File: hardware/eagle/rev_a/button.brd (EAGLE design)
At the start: 74 x 40 mm, 13 parts

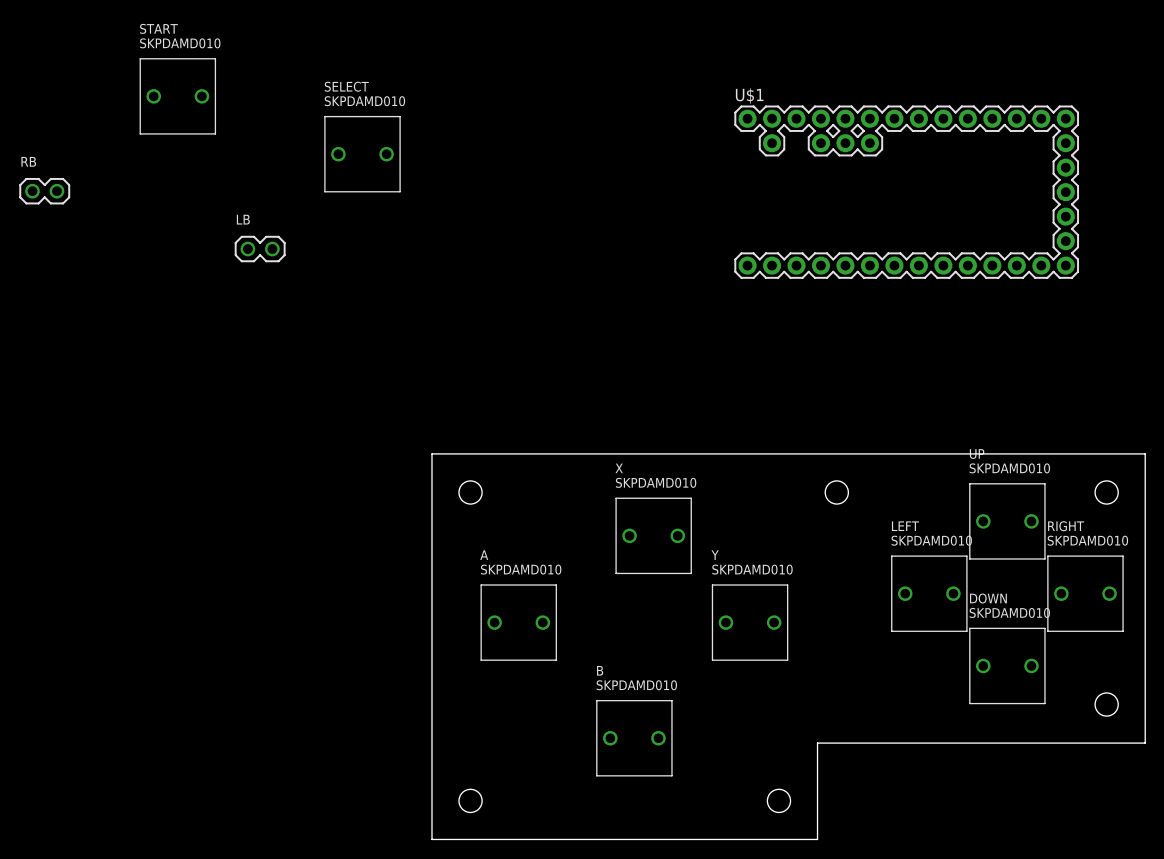
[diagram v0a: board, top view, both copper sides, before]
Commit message: First stab at button board Fits current body model, faceplate needs spacing of start/select
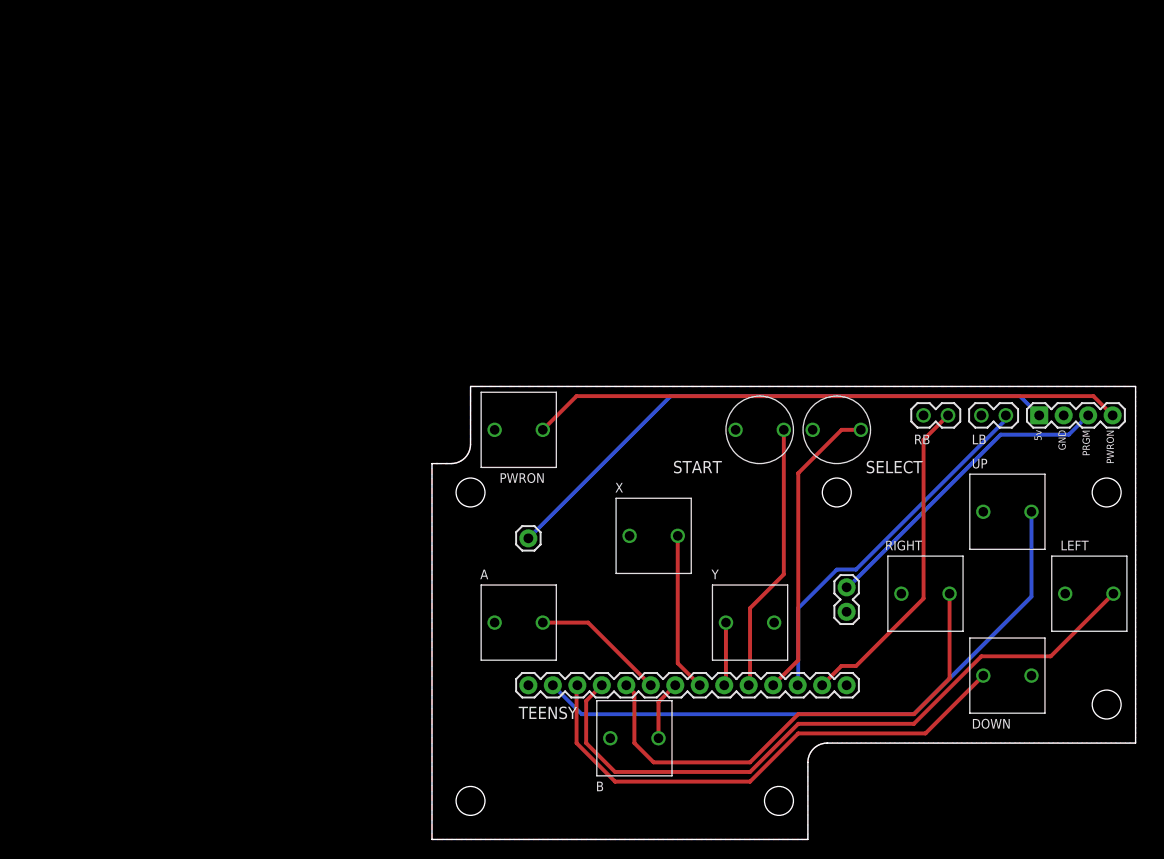
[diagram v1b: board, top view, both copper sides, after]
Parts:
- removed U$1: TEENSY_LC, BMO:TEENSY_LC
- added JP2: (no value), SparkFun-Connectors:1X04
- added PWRON: SKPDAMD010, switches:SKPDAMD010
- added TEENSY: TEENSY_LC, BMO:TEENSY_LC
- SELECT, START: value SKPDAMD010 -> EVQ11D09K; device switches:SKPDAMD010 -> BMO:EVQ11D09K
- moved RB 95.3 mm to (47.0, 40.0)
- moved LB 78.0 mm to (53.0, 40.0)
- moved START 69.6 mm to (30.0, 38.5)
- moved SELECT 56.9 mm to (38.0, 38.5)
- moved LEFT 16.6 mm to (64.2, 21.5)
- moved RIGHT 16.6 mm to (47.2, 21.5)
- moved DOWN 1.00 mm to (55.7, 13.0), turned to 180 degrees
- moved UP 1.00 mm to (55.7, 30.0)
- turned Y to 180 degrees
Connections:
- removed net N$7: A.P$2, U$1.6
- new net N$1: A.P$2, TEENSY.6
- new net N$2: JP2.4, PWRON.P$2
- new net PROGRAM: JP2.3, TEENSY.18
- new net VCC: JP2.1, TEENSY.22
- net GND: now also JP2.2, PWRON.P$1, TEENSY.1, TEENSY.17; no longer U$1.1, U$1.17, U$1.32
- net N$10: now also TEENSY.9; no longer U$1.9
- net N$11: now also TEENSY.10; no longer U$1.10
- net N$12: now also TEENSY.11; no longer U$1.11
- net N$13: now also TEENSY.12; no longer U$1.12
- net N$14: now also RB.2, TEENSY.13; no longer U$1.13
- net N$3: now also TEENSY.2; no longer U$1.2
- net N$4: now also TEENSY.3; no longer U$1.3
- net N$5: now also TEENSY.4; no longer U$1.4
- net N$6: now also TEENSY.5; no longer U$1.5
- net N$8: now also TEENSY.7; no longer U$1.7
- net N$9: now also TEENSY.8; no longer U$1.8
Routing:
- net N$5: track 0.00 -> 70.3 mm
- net N$3: track 0.00 -> 64.8 mm
- net N$2: track 0.00 -> 61.4 mm
- net VCC: track 0.00 -> 59.9 mm
- net N$4: track 0.00 -> 54.4 mm
- net N$6: track 0.00 -> 52.3 mm
- net N$13: track 0.00 -> 38.1 mm
- net N$14: track 0.00 -> 34.3 mm
- net PROGRAM: track 0.00 -> 32.4 mm
- net N$12: track 0.00 -> 31.4 mm
- net N$11: track 0.00 -> 28.0 mm
- net N$9: track 0.00 -> 16.4 mm
- net N$1: track 0.00 -> 13.9 mm
- net N$10: track 0.00 -> 6.57 mm
- net N$8: track 0.00 -> 6.22 mm
- added copper zone on layer 1, net GND
- added copper zone on layer 16, net GND
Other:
- board size 74 x 40 mm -> 73 x 47 mm
- board text added: "5v"
- board text added: "GND"
- board text added: "PRGM"
- board text added: "PWRON"

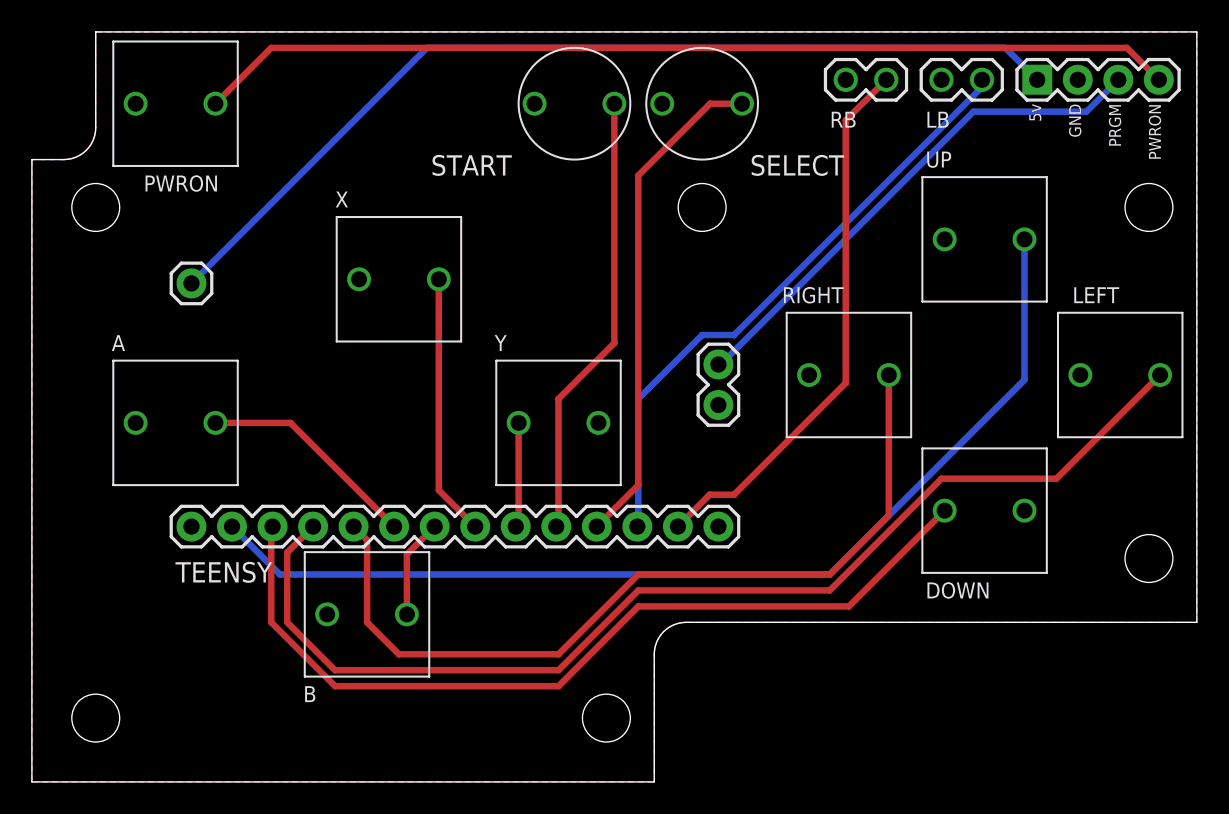
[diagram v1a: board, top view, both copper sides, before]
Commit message: Added boards for back buttons and charging/serial port Tweaks and redesigns for button/usb boards to fit in case better
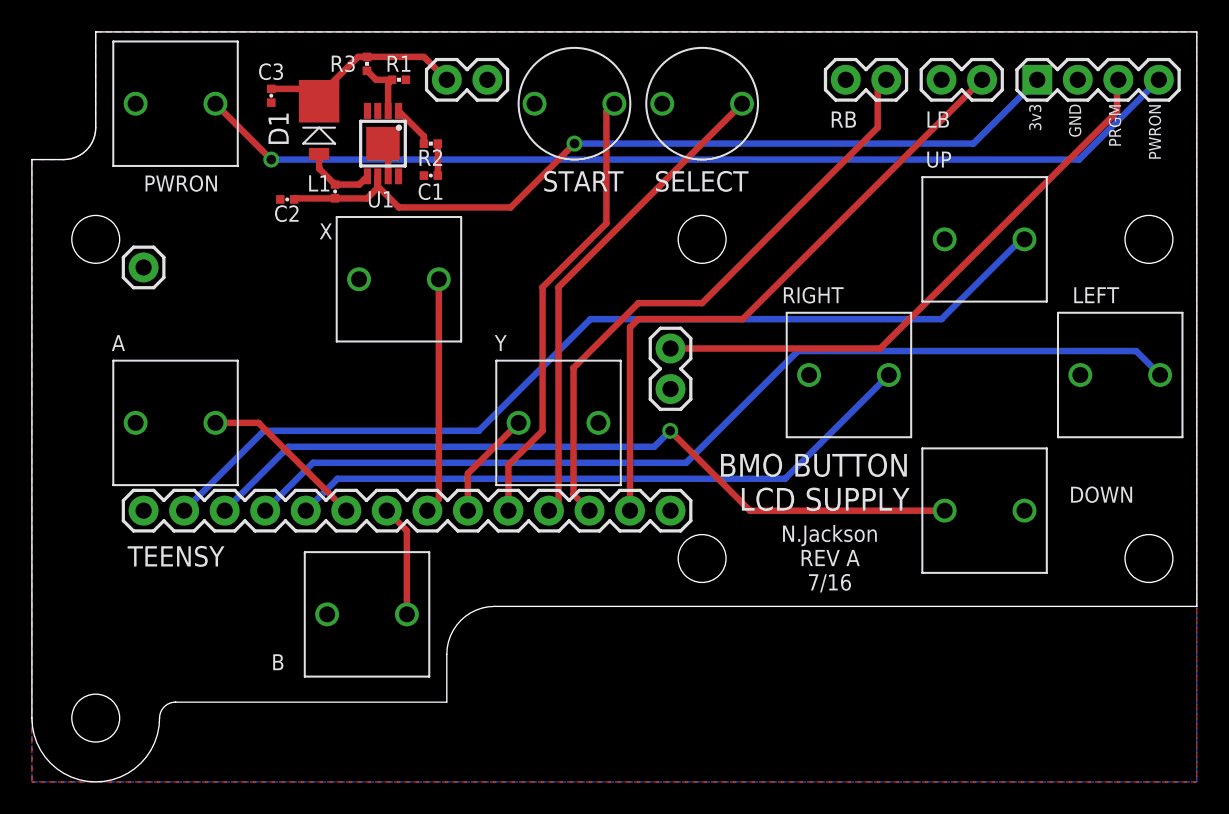
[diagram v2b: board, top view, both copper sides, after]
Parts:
- added C1: 2.2n, passives:0402_CAP
- added C2, C3: 22u, passives:0402_CAP
- added D1: MBRM140T3G, BMO:DO-216AA
- added JP1: (no value), SparkFun-Connectors:1X02
- added L1: 10u, passives:0402_CAP
- added R1: 7.5k, passives:0402_RES
- added R2: 24k, passives:0402_RES
- added R3: 40.2k, passives:0402_RES
- added U1: LM2622, BMO:MSOP8
- LB, RB: device umich:1X02 -> SparkFun-Connectors:1X02
- moved TEENSY 3.16 mm to (3.00, 13.0)
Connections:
- removed net VCC: JP2.1, TEENSY.22
- new net 3.3V: C2.1, JP2.1, L1.1, U1.6
- new net N$15: R2.2, U1.1
- new net N$16: D1.ANODE, L1.2, U1.5
- new net N$17: R1.2, R3.1, U1.2
- new net N$7: C1.1, R2.1
- new net VCC8V: C3.1, D1.CATHODE, JP1.1, R3.2
- net GND: now also C1.2, C2.2, C3.2, JP1.2, R1.1, U1.4, U1.7, U1.GND
- net N$13: now also RB.2; no longer LB.2
- net N$14: now also LB.2; no longer RB.2
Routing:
- net VCC: track 59.9 -> 0.00 mm
- net 3.3V: track 0.00 -> 52.1 mm, vias 0 -> 1
- net VCC8V: track 0.00 -> 13.3 mm
- net N$6: track 52.3 -> 40.1 mm
- net N$5: track 70.3 -> 60.8 mm
- net N$14: track 34.3 -> 40.0 mm
- net N$4: track 54.4 -> 49.3 mm, vias 0 -> 1
- net N$3: track 64.8 -> 59.7 mm
- net N$16: track 0.00 -> 4.57 mm
- net N$17: track 0.00 -> 3.85 mm
- net PROGRAM: track 32.4 -> 36.2 mm
- net N$1: track 13.9 -> 10.5 mm
- net N$15: track 0.00 -> 2.71 mm
- net GND: track 0.00 -> 2.18 mm
- net N$7: track 0.00 -> 2.00 mm
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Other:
- outline, holes or cut-outs redrawn
- board text added: "3v3"
- board text added: "8V"
- board text added: "BMO BUTTON LCD SUPPLY"
- board text added: "N.Jackson REV A 7/16"
- board text removed: "5v"
